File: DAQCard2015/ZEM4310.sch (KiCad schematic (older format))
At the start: 2 parts, among them P1 QTH-090-01-C-D-A, P2 QTH-090-01-C-D-A

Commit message: Adds power circuitry to DAQCard2015
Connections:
- net labels added: GNDdig
- net labels removed: GND_dig

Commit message: Replaces single ample with 4-channel varients. Greatly reducing part count
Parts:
- renumbered P2 to P1, P1 to P2
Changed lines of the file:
@@
 $EndDescr
 $Comp
-L QTH-090-01-C-D-A P1
+L QTH-090-01-C-D-A P2
 U 1 1 55C86FF8
 P 9700 6050
-F 0 "P1" H 9700 5950 50  0000 C CNN
+F 0 "P2" H 9700 5950 50  0000 C CNN
 F 1 "QTH-090-01-C-D-A" H 9700 6150 50  0000 C CNN
 F 2 "MODULE" H 9700 6050 50  0001 C CNN
@@
 CLKIN2n
 $Comp
-L QTH-090-01-C-D-A P2
+L QTH-090-01-C-D-A P1
 U 1 1 55C89057
 P 6650 6050
-F 0 "P2" H 6650 5950 50  0000 C CNN
+F 0 "P1" H 6650 5950 50  0000 C CNN
 F 1 "QTH-090-01-C-D-A" H 6650 6150 50  0000 C CNN
 F 2 "MODULE" H 6650 6050 50  0001 C CNN

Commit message: Finishes initial version of schematic(mostly). And adds a whole bunch of new footprints!
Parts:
- removed P1, P2: QTH-090-01-C-D-A, MODULE, symbol QTH-090-01-C-D-A
- added P1, P2: QTH-090-01-F-D-A, extras:QTH-090-XX-X-D-A, symbol QTH-090-01-F-D-A

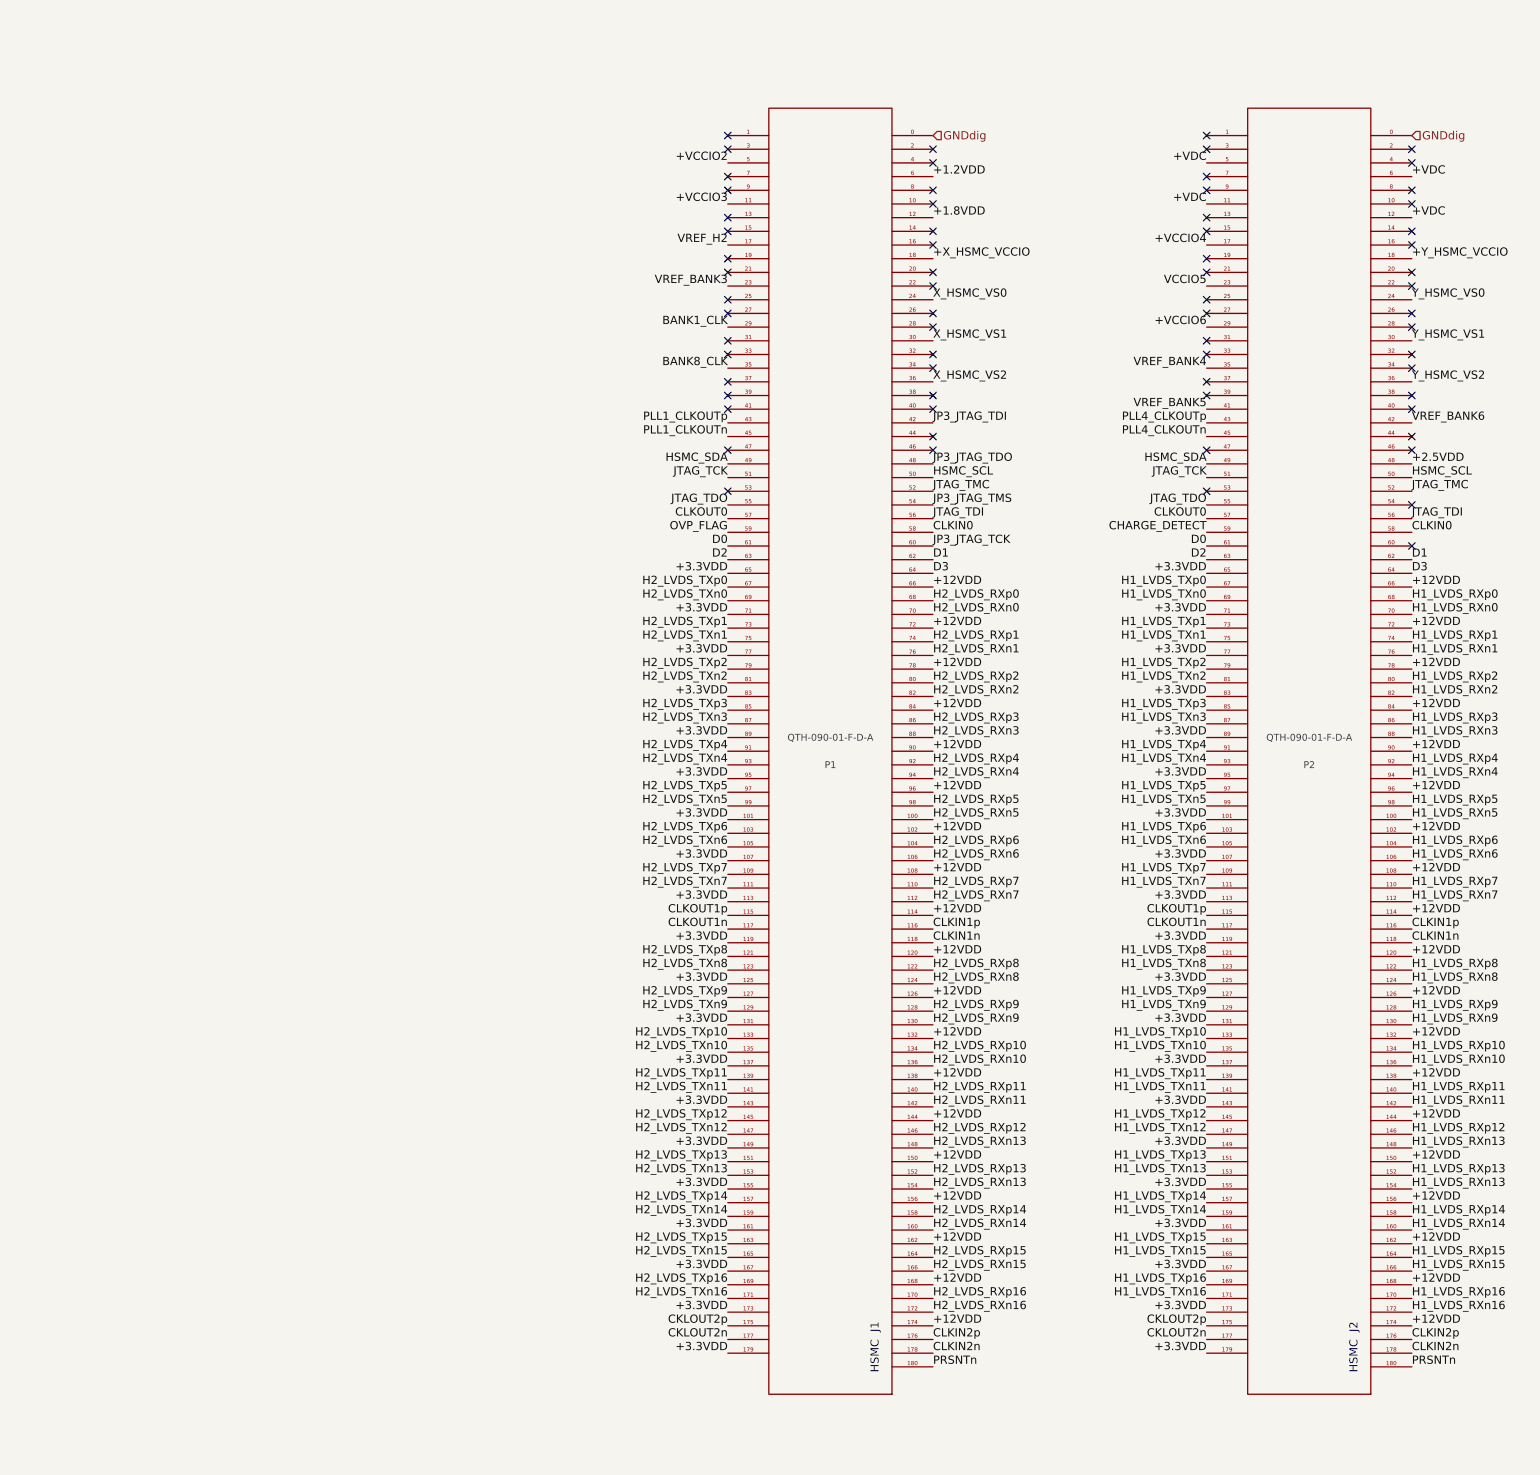
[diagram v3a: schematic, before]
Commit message: LVDS pins assigned and first round routing finished, work on 3d models
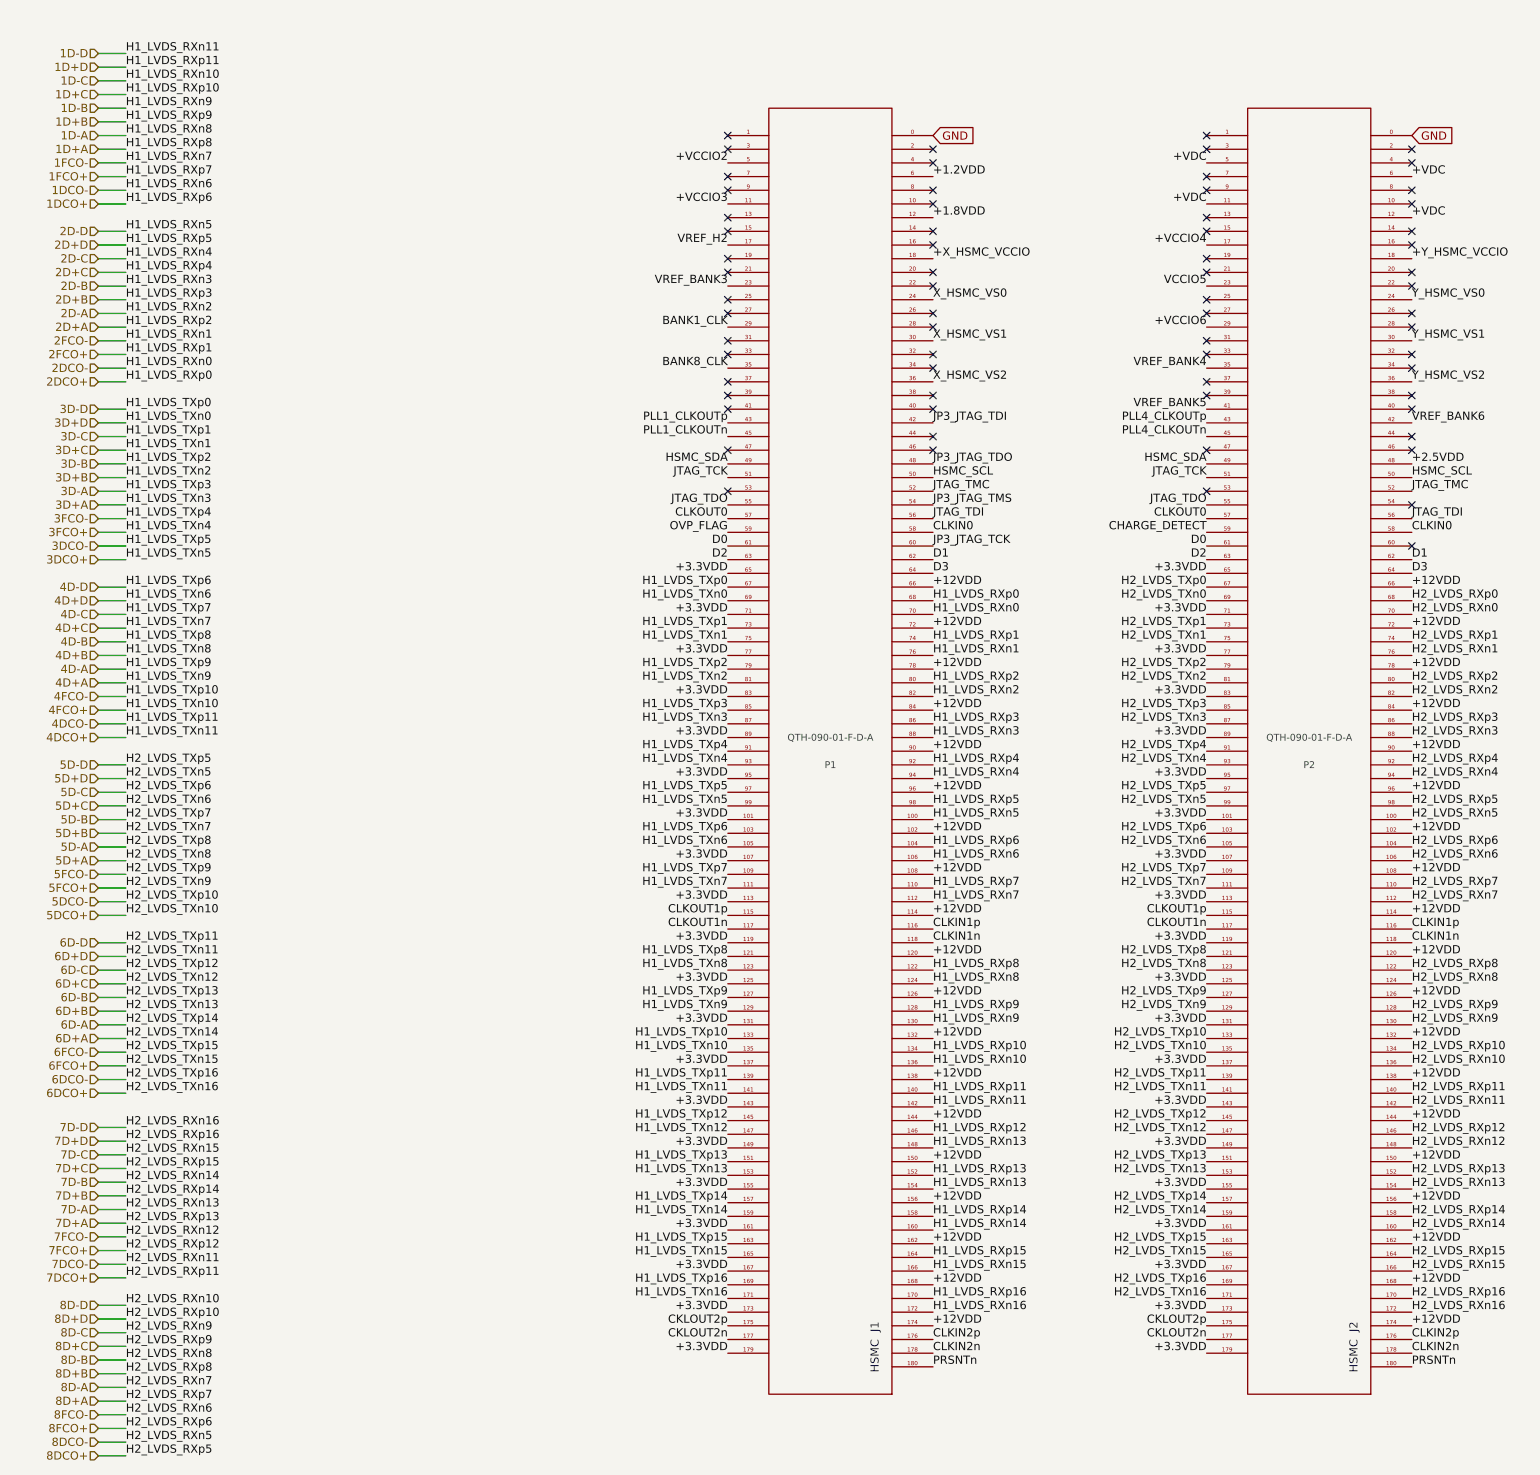
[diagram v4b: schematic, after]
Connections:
- net H1_LVDS_RXn0 is gone; now on net H2_LVDS_RXn0: P2.70
- net H1_LVDS_RXn1 is gone; now on net H2_LVDS_RXn1: P2.76
- net H1_LVDS_RXn2 is gone; now on net H2_LVDS_RXn2: P2.82
- net H1_LVDS_RXn3 is gone; now on net H2_LVDS_RXn3: P2.88
- net H1_LVDS_RXn4 is gone; now on net H2_LVDS_RXn4: P2.94
- net H1_LVDS_RXp0 is gone; now on net H2_LVDS_RXp0: P2.68
- net H1_LVDS_RXp1 is gone; now on net H2_LVDS_RXp1: P2.74
- net H1_LVDS_RXp2 is gone; now on net H2_LVDS_RXp2: P2.80
- net H1_LVDS_RXp3 is gone; now on net H2_LVDS_RXp3: P2.86
- net H1_LVDS_RXp4 is gone; now on net H2_LVDS_RXp4: P2.92
- net H1_LVDS_TXn0 is gone; now on net H2_LVDS_TXn0: P2.69
- net H1_LVDS_TXn1 is gone; now on net H2_LVDS_TXn1: P2.75
- net H1_LVDS_TXn2 is gone; now on net H2_LVDS_TXn2: P2.81
- net H1_LVDS_TXn3 is gone; now on net H2_LVDS_TXn3: P2.87
- net H1_LVDS_TXn4 is gone; now on net H2_LVDS_TXn4: P2.93
- net H1_LVDS_TXp0 is gone; now on net H2_LVDS_TXp0: P2.67
- net H1_LVDS_TXp1 is gone; now on net H2_LVDS_TXp1: P2.73
- net H1_LVDS_TXp2 is gone; now on net H2_LVDS_TXp2: P2.79
- net H1_LVDS_TXp3 is gone; now on net H2_LVDS_TXp3: P2.85
- net H1_LVDS_TXp4 is gone; now on net H2_LVDS_TXp4: P2.91
- net H2_LVDS_RXn13 is gone; now on net H1_LVDS_RXn13: P1.148, P1.154
- net H2_LVDS_RXn14 is gone; now on net H1_LVDS_RXn14: P1.160
- net H2_LVDS_RXn15 is gone; now on net H1_LVDS_RXn15: P1.166
- net H2_LVDS_RXn16 is gone; now on net H1_LVDS_RXn16: P1.172
- net H2_LVDS_RXp12 is gone; now on net H1_LVDS_RXp12: P1.146
- net H2_LVDS_RXp13 is gone; now on net H1_LVDS_RXp13: P1.152
- net H2_LVDS_RXp14 is gone; now on net H1_LVDS_RXp14: P1.158
- net H2_LVDS_RXp15 is gone; now on net H1_LVDS_RXp15: P1.164
- net H2_LVDS_RXp16 is gone; now on net H1_LVDS_RXp16: P1.170
- net H2_LVDS_TXn12 is gone; now on net H1_LVDS_TXn12: P1.147
- net H2_LVDS_TXn13 is gone; now on net H1_LVDS_TXn13: P1.153
- net H2_LVDS_TXn14 is gone; now on net H1_LVDS_TXn14: P1.159
- net H2_LVDS_TXn15 is gone; now on net H1_LVDS_TXn15: P1.165
- net H2_LVDS_TXn16 is gone; now on net H1_LVDS_TXn16: P1.171
- net H2_LVDS_TXp12 is gone; now on net H1_LVDS_TXp12: P1.145
- net H2_LVDS_TXp13 is gone; now on net H1_LVDS_TXp13: P1.151
- net H2_LVDS_TXp14 is gone; now on net H1_LVDS_TXp14: P1.157
- net H2_LVDS_TXp15 is gone; now on net H1_LVDS_TXp15: P1.163
- net H2_LVDS_TXp16 is gone; now on net H1_LVDS_TXp16: P1.169
- net H1_LVDS_RXn13: no longer P2.148, P2.154
- net H1_LVDS_RXn14: no longer P2.160
- net H1_LVDS_RXn15: no longer P2.166
- net H1_LVDS_RXn16: no longer P2.172
- net H1_LVDS_RXp12: no longer P2.146
- net H1_LVDS_RXp13: no longer P2.152
- net H1_LVDS_RXp14: no longer P2.158
- net H1_LVDS_RXp15: no longer P2.164
- net H1_LVDS_RXp16: no longer P2.170
- net H1_LVDS_TXn12: no longer P2.147
- net H1_LVDS_TXn13: no longer P2.153
- net H1_LVDS_TXn14: no longer P2.159
- net H1_LVDS_TXn15: no longer P2.165
- net H1_LVDS_TXn16: no longer P2.171
- net H1_LVDS_TXp12: no longer P2.145
- net H1_LVDS_TXp13: no longer P2.151
- net H1_LVDS_TXp14: no longer P2.157
- net H1_LVDS_TXp15: no longer P2.163
- net H1_LVDS_TXp16: no longer P2.169
- net H2_LVDS_RXn0: no longer P1.70
- net H2_LVDS_RXn1: no longer P1.76
- net H2_LVDS_RXn2: no longer P1.82
- net H2_LVDS_RXn3: no longer P1.88
- net H2_LVDS_RXn4: no longer P1.94
- net H2_LVDS_RXp0: no longer P1.68
- net H2_LVDS_RXp1: no longer P1.74
- net H2_LVDS_RXp2: no longer P1.80
- net H2_LVDS_RXp3: no longer P1.86
- net H2_LVDS_RXp4: no longer P1.92
- net H2_LVDS_TXn0: no longer P1.69
- net H2_LVDS_TXn1: no longer P1.75
- net H2_LVDS_TXn2: no longer P1.81
- net H2_LVDS_TXn3: no longer P1.87
- net H2_LVDS_TXn4: no longer P1.93
- net H2_LVDS_TXp0: no longer P1.67
- net H2_LVDS_TXp1: no longer P1.73
- net H2_LVDS_TXp2: no longer P1.79
- net H2_LVDS_TXp3: no longer P1.85
- net H2_LVDS_TXp4: no longer P1.91
- net GNDdig renamed GND
- net H1_LVDS_RXn10 renamed 8D-D
- net H1_LVDS_RXn11 renamed 7DCO-
- net H1_LVDS_RXn5 renamed 8DCO-
- net H1_LVDS_RXn6 renamed 8FCO-
- net H1_LVDS_RXn7 renamed 8D-A
- net H1_LVDS_RXn8 renamed 8D-B
- net H1_LVDS_RXn9 renamed 8D-C
- net H1_LVDS_RXp10 renamed 8D+D
- net H1_LVDS_RXp11 renamed 7DCO+
- net H1_LVDS_RXp5 renamed 8DCO+
- net H1_LVDS_RXp6 renamed 8FCO+
- net H1_LVDS_RXp7 renamed 8D+A
- net H1_LVDS_RXp8 renamed 8D+B
- net H1_LVDS_RXp9 renamed 8D+C
- net H1_LVDS_TXn10 renamed 5DCO+
- net H1_LVDS_TXn11 renamed 6D+D
- net H1_LVDS_TXn5 renamed 5D+D
- net H1_LVDS_TXn6 renamed 5D+C
- net H1_LVDS_TXn7 renamed 5D+B
- net H1_LVDS_TXn8 renamed 5D+A
- net H1_LVDS_TXn9 renamed 5FCO+
- net H1_LVDS_TXp10 renamed 5DCO-
- net H1_LVDS_TXp11 renamed 6D-D
- net H1_LVDS_TXp5 renamed 5D-D
- net H1_LVDS_TXp6 renamed 5D-C
- net H1_LVDS_TXp7 renamed 5D-B
- net H1_LVDS_TXp8 renamed 5D-A
- net H1_LVDS_TXp9 renamed 5FCO-
- net H2_LVDS_RXn10 renamed 1D-C
- net H2_LVDS_RXn11 renamed 1D-D
- net H2_LVDS_RXn5 renamed 2D-D
- net H2_LVDS_RXn6 renamed 1DCO-
- net H2_LVDS_RXn7 renamed 1FCO-
- net H2_LVDS_RXn8 renamed 1D-A
- net H2_LVDS_RXn9 renamed 1D-B
- net H2_LVDS_RXp10 renamed 1D+C
- net H2_LVDS_RXp11 renamed 1D+D
- net H2_LVDS_RXp5 renamed 2D+D
- net H2_LVDS_RXp6 renamed 1DCO+
- net H2_LVDS_RXp7 renamed 1FCO+
- net H2_LVDS_RXp8 renamed 1D+A
- net H2_LVDS_RXp9 renamed 1D+B
- net H2_LVDS_TXn10 renamed 4FCO+
- net H2_LVDS_TXn11 renamed 4DCO+
- net H2_LVDS_TXn5 renamed 3DCO+
- net H2_LVDS_TXn6 renamed 4D+D
- net H2_LVDS_TXn7 renamed 4D+C
- net H2_LVDS_TXn8 renamed 4D+B
- net H2_LVDS_TXn9 renamed 4D+A
- net H2_LVDS_TXp10 renamed 4FCO-
- net H2_LVDS_TXp11 renamed 4DCO-
- net H2_LVDS_TXp5 renamed 3DCO-
- net H2_LVDS_TXp6 renamed 4D-D
- net H2_LVDS_TXp7 renamed 4D-C
- net H2_LVDS_TXp8 renamed 4D-B
- net H2_LVDS_TXp9 renamed 4D-A
- new net 2D+A: P1.80
- new net 2D+B: P1.86
- new net 2D+C: P1.92
- new net 2D-A: P1.82
- new net 2D-B: P1.88
- new net 2D-C: P1.94
- new net 2DCO+: P1.68
- new net 2DCO-: P1.70
- new net 2FCO+: P1.74
- new net 2FCO-: P1.76
- new net 3D+A: P1.87
- new net 3D+B: P1.81
- new net 3D+C: P1.75
- new net 3D+D: P1.69
- new net 3D-A: P1.85
- new net 3D-B: P1.79
- new net 3D-C: P1.73
- new net 3D-D: P1.67
- new net 3FCO+: P1.93
- new net 3FCO-: P1.91
- new net 6D+A: P2.159
- new net 6D+B: P2.153
- new net 6D+C: P2.147
- new net 6D-A: P2.157
- new net 6D-B: P2.151
- new net 6D-C: P2.145
- new net 6DCO+: P2.171
- new net 6DCO-: P2.169
- new net 6FCO+: P2.165
- new net 6FCO-: P2.163
- new net 7D+A: P2.152
- new net 7D+B: P2.158
- new net 7D+C: P2.164
- new net 7D+D: P2.170
- new net 7D-A: P2.154
- new net 7D-B: P2.160
- new net 7D-C: P2.166
- new net 7D-D: P2.172
- new net 7FCO+: P2.146
- new net 7FCO-: P2.148

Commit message: Various updates to DAQ board focusing on power system
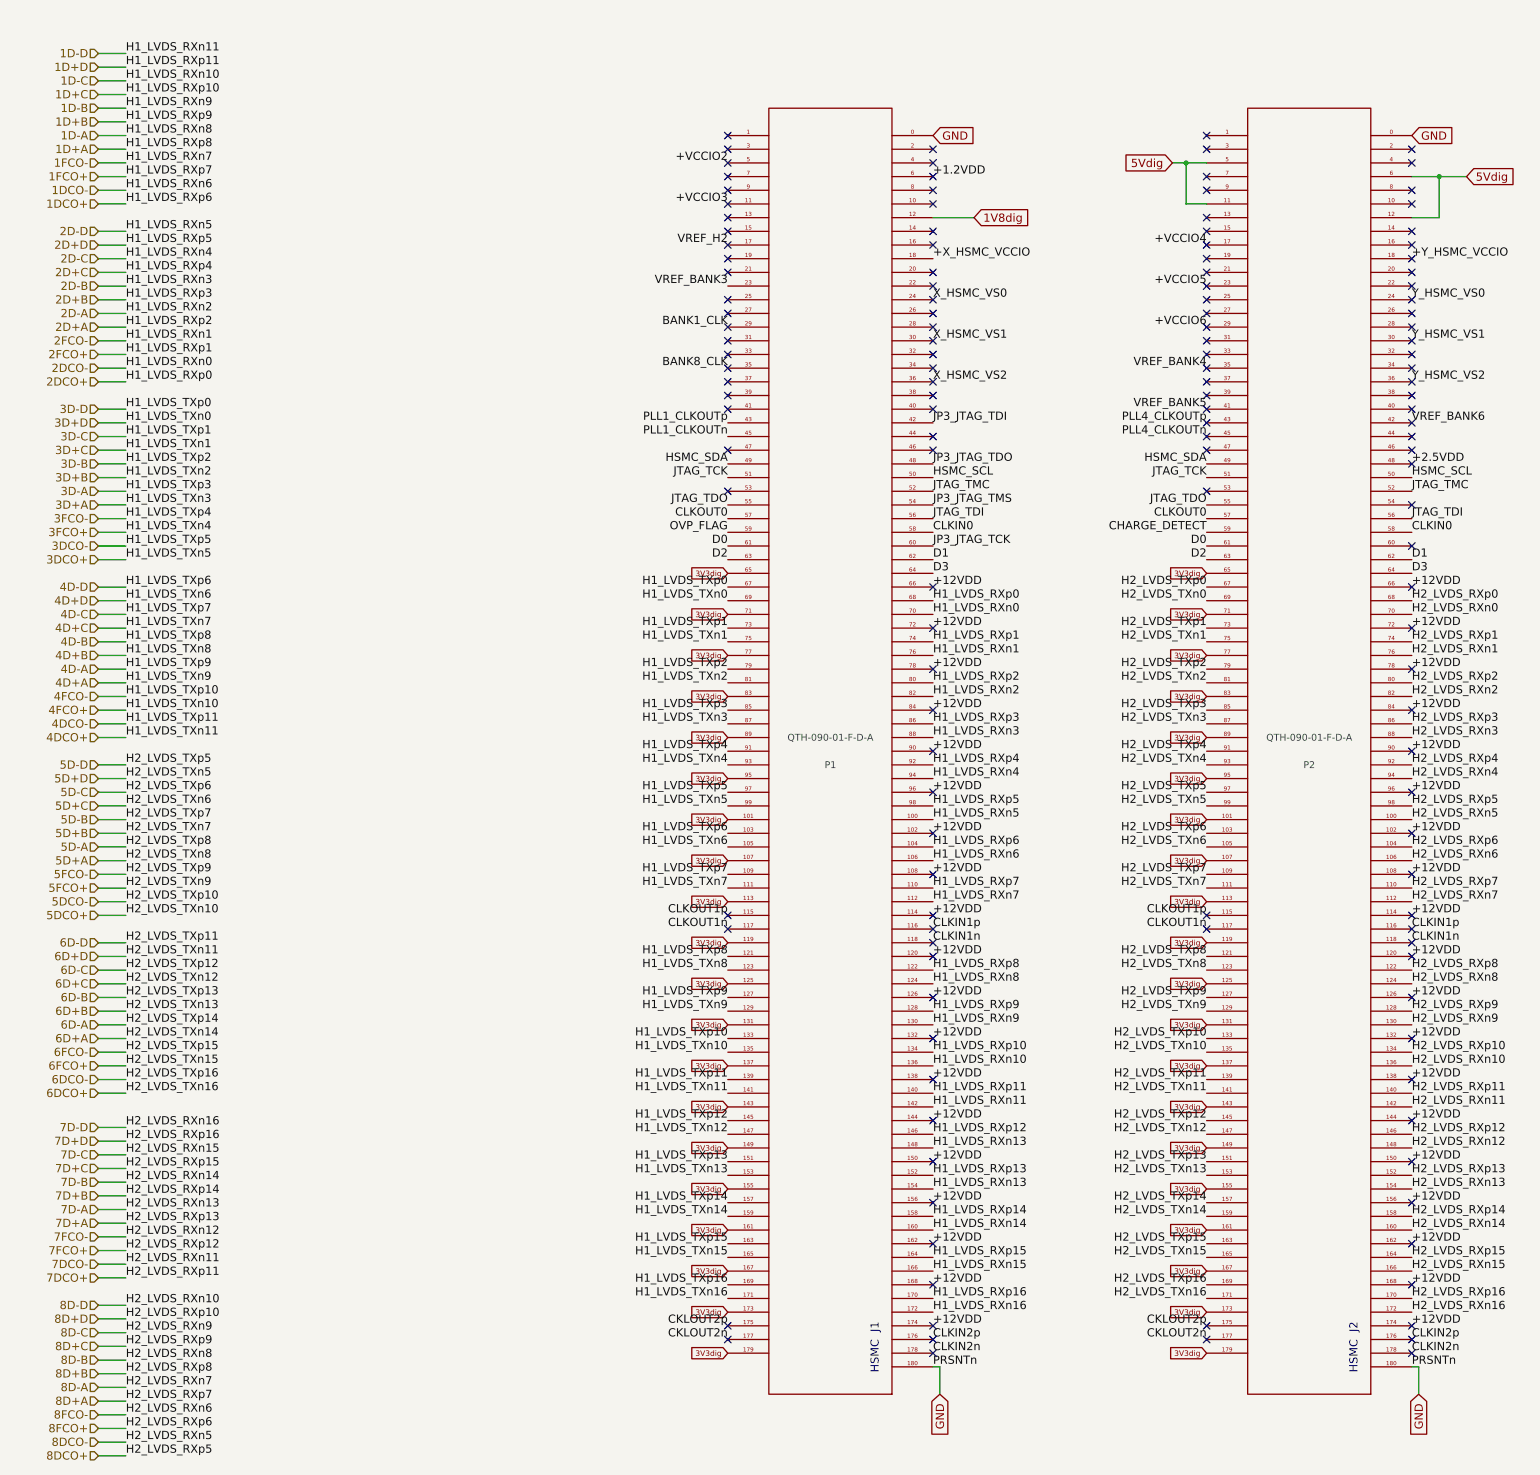
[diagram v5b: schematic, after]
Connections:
- net PRSNTn is gone; now on net GND: P1.180, P2.180
- net +1.8VDD renamed 1V8dig
- net +3.3VDD renamed 3V3dig
- net +VDC renamed 5Vdig
- net VCCIO5 renamed +VCCIO5
- no-connect marks 67 -> 143
